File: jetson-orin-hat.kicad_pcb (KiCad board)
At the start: 2 copper layers, 4 parts, among them J1 Jetson, J2 I2C0, J3 I2C1, J4 UART

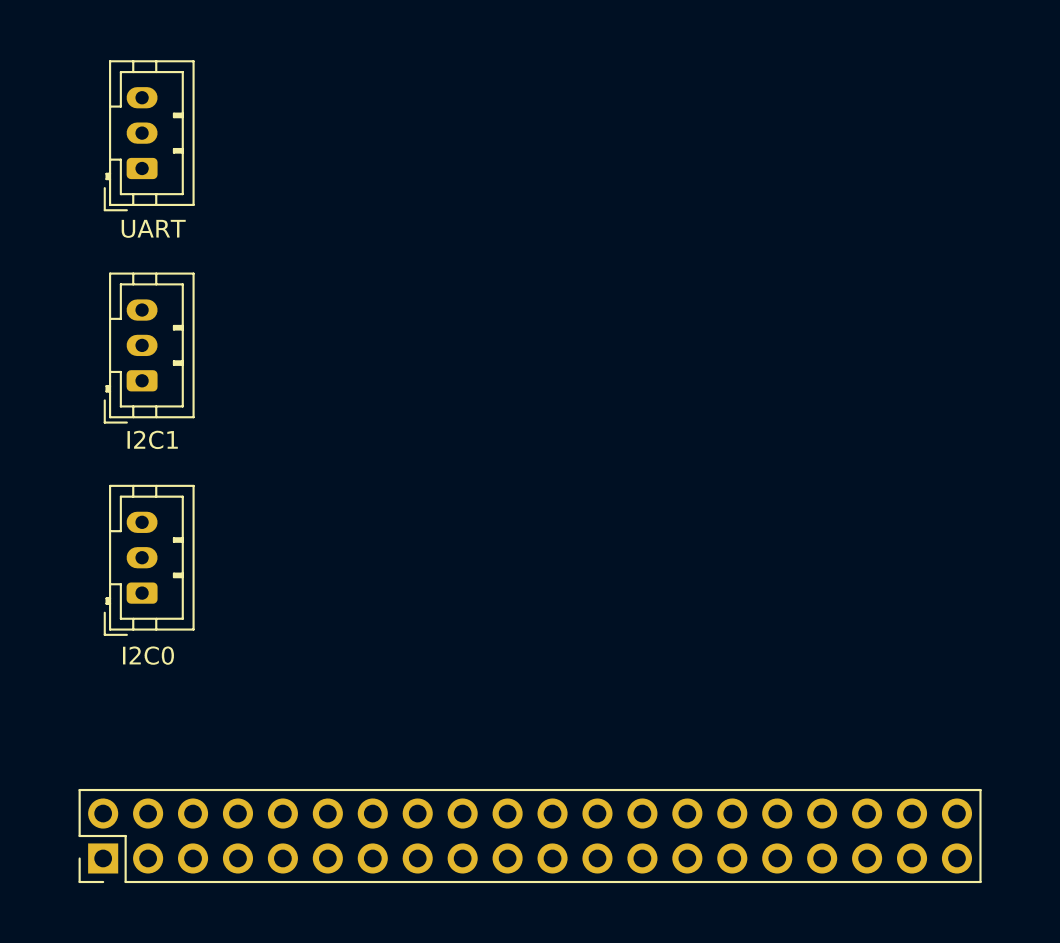
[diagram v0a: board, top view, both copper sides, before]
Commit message: done board outline
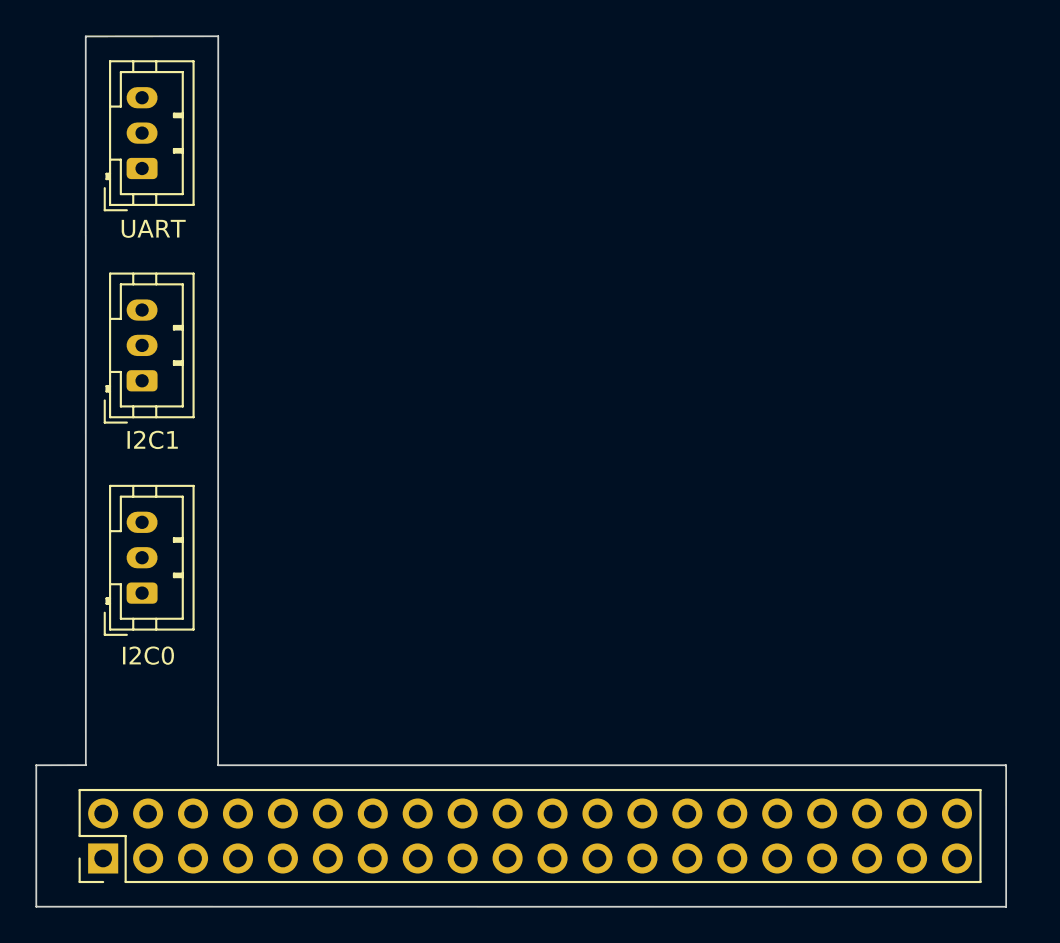
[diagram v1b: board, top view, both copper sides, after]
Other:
- board outline added: 54.8 x 49.2 mm
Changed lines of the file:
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@@
     )
   )
-  (gr_line (start 10 109.918) (end 150 109.918)
-    (stroke (width 0.1) (type default)) (layer "F.Fab"))
-  (gr_line (start 64.04 56.134) (end 64.04 150.622)
-    (stroke (width 0.1) (type default)) (layer "F.Fab"))
-  (gr_line (start 118.856 56.134) (end 118.856 150.622)
-    (stroke (width 0.1) (type default)) (layer "F.Fab"))
-  (gr_line (start 9.248 101.918) (end 149.248 101.918)
-    (stroke (width 0.1) (type default)) (layer "F.Fab"))
-  (gr_line (start 23.876 60.722) (end 118.364 60.722)
-    (stroke (width 0.1) (type default)) (layer "F.Fab"))
-  (gr_line (start 74.323589 37.418391) (end 74.323589 131.906391)
-    (stroke (width 0.1) (type default)) (layer "F.Fab"))
-  (gr_line (start 66.838939 37.418391) (end 66.838939 131.906391)
-    (stroke (width 0.1) (type default)) (layer "F.Fab"))
+  (gr_line (start 66.839214 101.911936) (end 64.036467 101.918446)
+    (stroke (width 0.1) (type default)) (layer "Edge.Cuts"))
+  (gr_line (start 64.040025 109.913995) (end 118.856876 109.918838)
+    (stroke (width 0.1) (type default)) (layer "Edge.Cuts"))
+  (gr_line (start 64.036467 101.918446) (end 64.040025 109.913995)
+    (stroke (width 0.1) (type default)) (layer "Edge.Cuts"))
+  (gr_line (start 74.322809 60.71386) (end 66.834277 60.721819)
+    (stroke (width 0.1) (type default)) (layer "Edge.Cuts"))
+  (gr_line (start 74.314645 101.917415) (end 74.322809 60.71386)
+    (stroke (width 0.1) (type default)) (layer "Edge.Cuts"))
+  (gr_line (start 118.856876 109.918838) (end 118.855393 101.918006)
+    (stroke (width 0.1) (type default)) (layer "Edge.Cuts"))
+  (gr_line (start 66.834277 60.721819) (end 66.839214 101.911936)
+    (stroke (width 0.1) (type default)) (layer "Edge.Cuts"))
+  (gr_line (start 118.855393 101.918006) (end 74.314645 101.917415)
+    (stroke (width 0.1) (type default)) (layer "Edge.Cuts"))
   (gr_line (start 64.262 145.288) (end 64.262 145.288)
     (stroke (width 0.1) (type default)) (layer "F.Fab"))
+  (gr_line (start 10 109.918) (end 150 109.918)
+    (stroke (width 0.1) (type default)) (layer "User.2"))
+  (gr_line (start 64.04 56.134) (end 64.04 150.622)
+    (stroke (width 0.1) (type default)) (layer "User.2"))
+  (gr_line (start 118.856 56.134) (end 118.856 150.622)
+    (stroke (width 0.1) (type default)) (layer "User.2"))
+  (gr_line (start 9.248 101.918) (end 149.248 101.918)
+    (stroke (width 0.1) (type default)) (layer "User.2"))
+  (gr_line (start 23.876 60.722) (end 118.364 60.722)
+    (stroke (width 0.1) (type default)) (layer "User.2"))
+  (gr_line (start 74.323589 37.418391) (end 74.323589 131.906391)
+    (stroke (width 0.1) (type default)) (layer "User.2"))
+  (gr_line (start 66.838939 37.418391) (end 66.838939 131.906391)
+    (stroke (width 0.1) (type default)) (layer "User.2"))
 )

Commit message: edit size
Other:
- board size 54.8 x 49.2 mm -> 55.8 x 49.2 mm
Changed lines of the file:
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@@
     )
   )
-  (gr_line (start 66.839214 101.911936) (end 64.036467 101.918446)
-    (stroke (width 0.1) (type default)) (layer "Edge.Cuts"))
-  (gr_line (start 64.040025 109.913995) (end 118.856876 109.918838)
-    (stroke (width 0.1) (type default)) (layer "Edge.Cuts"))
-  (gr_line (start 64.036467 101.918446) (end 64.040025 109.913995)
-    (stroke (width 0.1) (type default)) (layer "Edge.Cuts"))
-  (gr_line (start 74.322809 60.71386) (end 66.834277 60.721819)
-    (stroke (width 0.1) (type default)) (layer "Edge.Cuts"))
-  (gr_line (start 74.314645 101.917415) (end 74.322809 60.71386)
-    (stroke (width 0.1) (type default)) (layer "Edge.Cuts"))
-  (gr_line (start 118.856876 109.918838) (end 118.855393 101.918006)
-    (stroke (width 0.1) (type default)) (layer "Edge.Cuts"))
-  (gr_line (start 66.834277 60.721819) (end 66.839214 101.911936)
-    (stroke (width 0.1) (type default)) (layer "Edge.Cuts"))
-  (gr_line (start 118.855393 101.918006) (end 74.314645 101.917415)
-    (stroke (width 0.1) (type default)) (layer "Edge.Cuts"))
+  (gr_poly
+    (pts
+      (xy 66.839214 101.911936)
+      (xy 66.834277 60.721819)
+      (xy 74.322809 60.71386)
+      (xy 74.314645 101.917415)
+      (xy 119.871393 101.918006)
+      (xy 119.872876 109.918838)
+      (xy 64.040025 109.913995)
+      (xy 64.036467 101.918446)
+    )
+    (stroke (width 0.1) (type solid)) (fill none) (layer "Edge.Cuts"))
   (gr_line (start 64.262 145.288) (end 64.262 145.288)
     (stroke (width 0.1) (type default)) (layer "F.Fab"))
@@
   (gr_line (start 64.04 56.134) (end 64.04 150.622)
     (stroke (width 0.1) (type default)) (layer "User.2"))
-  (gr_line (start 118.856 56.134) (end 118.856 150.622)
+  (gr_line (start 119.856 56.134) (end 119.856 150.622)
     (stroke (width 0.1) (type default)) (layer "User.2"))
   (gr_line (start 9.248 101.918) (end 149.248 101.918)

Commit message: made fit
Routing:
- net I2C0-SDA: track 0.00 -> 46.7 mm
- net UART-RX: track 0.00 -> 46.1 mm, vias 0 -> 1
- net I2C0-SCL: track 0.00 -> 43.8 mm
- net UART-TX: track 0.00 -> 42.7 mm
- net I2C1-SCL: track 0.00 -> 35.2 mm, vias 0 -> 1
- net I2C1-SDA: track 0.00 -> 31.2 mm
- added copper zone on B.Cu, net GND
- added copper zone on F.Cu, net GND
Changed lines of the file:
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@@
   (gr_line (start 66.838939 37.418391) (end 66.838939 131.906391)
     (stroke (width 0.1) (type default)) (layer "User.2"))
+  (segment (start 69.088 105.918) (end 69.088 102.616) (width 0.25) (layer "B.Cu") (net 3))
+  (segment (start 70.358 107.188) (end 69.088 105.918) (width 0.25) (layer "B.Cu") (net 3))
+  (segment (start 67.564 80.642) (end 70.018 78.188) (width 0.25) (layer "B.Cu") (net 3))
+  (segment (start 69.088 102.616) (end 67.564 101.092) (width 0.25) (layer "B.Cu") (net 3))
+  (segment (start 67.564 101.092) (end 67.564 80.642) (width 0.25) (layer "B.Cu") (net 3))
+  (segment (start 70.612 84.582) (end 71.218 83.976) (width 0.25) (layer "F.Cu") (net 5))
+  (segment (start 71.218 77.388) (end 70.018 76.188) (width 0.25) (layer "F.Cu") (net 5))
+  (segment (start 71.218 83.976) (end 71.218 77.388) (width 0.25) (layer "F.Cu") (net 5))
+  (via (at 70.612 84.582) (size 0.8) (drill 0.4) (layers "F.Cu" "B.Cu") (net 5))
+  (segment (start 69.596 84.582) (end 68.326 85.852) (width 0.25) (layer "B.Cu") (net 5))
+  (segment (start 70.612 84.582) (end 69.596 84.582) (width 0.25) (layer "B.Cu") (net 5))
+  (segment (start 68.326 85.852) (end 68.326 100.838) (width 0.25) (layer "B.Cu") (net 5))
+  (segment (start 71.616598 104.128598) (end 71.616598 105.906598) (width 0.25) (layer "B.Cu") (net 5))
+  (segment (start 68.326 100.838) (end 71.616598 104.128598) (width 0.25) (layer "B.Cu") (net 5))
+  (segment (start 71.616598 105.906598) (end 72.898 107.188) (width 0.25) (layer "B.Cu") (net 5))
+  (segment (start 75.438 104.648) (end 67.564 96.774) (width 0.25) (layer "F.Cu") (net 8))
+  (segment (start 67.564 68.642) (end 70.018 66.188) (width 0.25) (layer "F.Cu") (net 8))
+  (segment (start 67.564 96.774) (end 67.564 68.642) (width 0.25) (layer "F.Cu") (net 8))
+  (segment (start 77.978 104.648) (end 75.946 102.616) (width 0.25) (layer "F.Cu") (net 9))
+  (segment (start 68.326 96.52) (end 68.326 69.596) (width 0.25) (layer "F.Cu") (net 9))
+  (segment (start 74.422 102.616) (end 68.326 96.52) (width 0.25) (layer "F.Cu") (net 9))
+  (segment (start 75.946 102.616) (end 74.422 102.616) (width 0.25) (layer "F.Cu") (net 9))
+  (via (at 68.326 69.596) (size 0.8) (drill 0.4) (layers "F.Cu" "B.Cu") (net 9))
+  (segment (start 68.326 69.596) (end 68.326 65.88) (width 0.25) (layer "B.Cu") (net 9))
+  (segment (start 68.326 65.88) (end 70.018 64.188) (width 0.25) (layer "B.Cu") (net 9))
+  (segment (start 71.628 91.798) (end 70.018 90.188) (width 0.25) (layer "B.Cu") (net 23))
+  (segment (start 74.188266 107.716266) (end 74.188266 103.986424) (width 0.25) (layer "B.Cu") (net 23))
+  (segment (start 100.838 107.188) (end 99.568596 108.457404) (width 0.25) (layer "B.Cu") (net 23))
+  (segment (start 99.568596 108.457404) (end 74.929404 108.457404) (width 0.25) (layer "B.Cu") (net 23))
+  (segment (start 74.188266 103.986424) (end 71.628 101.426158) (width 0.25) (layer "B.Cu") (net 23))
+  (segment (start 71.628 101.426158) (end 71.628 91.798) (width 0.25) (layer "B.Cu") (net 23))
+  (segment (start 74.929404 108.457404) (end 74.188266 107.716266) (width 0.25) (layer "B.Cu") (net 23))
+  (segment (start 72.898 101.6) (end 72.898 91.068) (width 0.25) (layer "B.Cu") (net 24))
+  (segment (start 72.898 91.068) (end 70.018 88.188) (width 0.25) (layer "B.Cu") (net 24))
+  (segment (start 74.168 102.87) (end 72.898 101.6) (width 0.25) (layer "B.Cu") (net 24))
+  (segment (start 100.838 104.648) (end 99.06 102.87) (width 0.25) (layer "B.Cu") (net 24))
+  (segment (start 99.06 102.87) (end 74.168 102.87) (width 0.25) (layer "B.Cu") (net 24))
+  (zone (net 6) (net_name "GND") (layers "F&B.Cu") (name "GND") (hatch edge 0.5)
+    (connect_pads yes (clearance 0.5))
+    (min_thickness 0.25) (filled_areas_thickness no)
+    (fill yes (thermal_gap 0.5) (thermal_bridge_width 0.5))
+    (polygon
+      (pts
+        (xy 66.839214 101.911936)
+        (xy 66.834277 60.721819)
+        (xy 74.322809 60.71386)
+        (xy 74.314645 101.917415)
+        (xy 119.871393 101.918006)
+        (xy 119.872876 109.918838)
+        (xy 64.040025 109.913995)
+        (xy 64.036467 101.918446)
+      )
+    )
+  )
 )
